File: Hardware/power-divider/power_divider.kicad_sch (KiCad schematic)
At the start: 22 parts

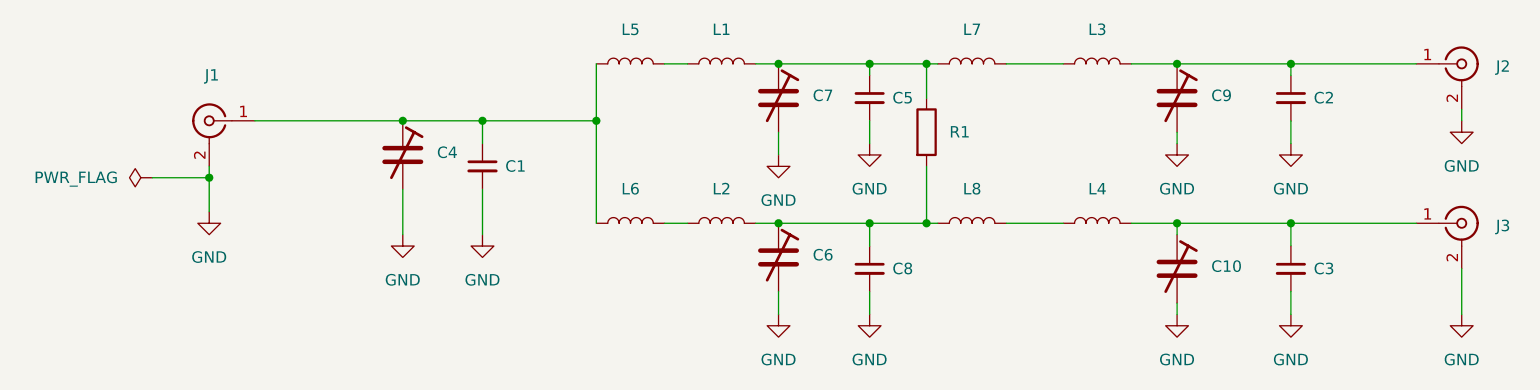
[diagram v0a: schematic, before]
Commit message: PD: Silkscreen Color Tweak
- Changed bottom silkscreen to green
- Aligned board edges and fill polygon to grid
- Rounded the corners
- Added box for label
- Moved R1 slightly closer
- Increased default netclass clearance from 0.2 to 0.6mm
- Set polygon clearance to 0 to fill to edge of holes
- Added SMA connector models
- Fixed Schematic-PCB parity
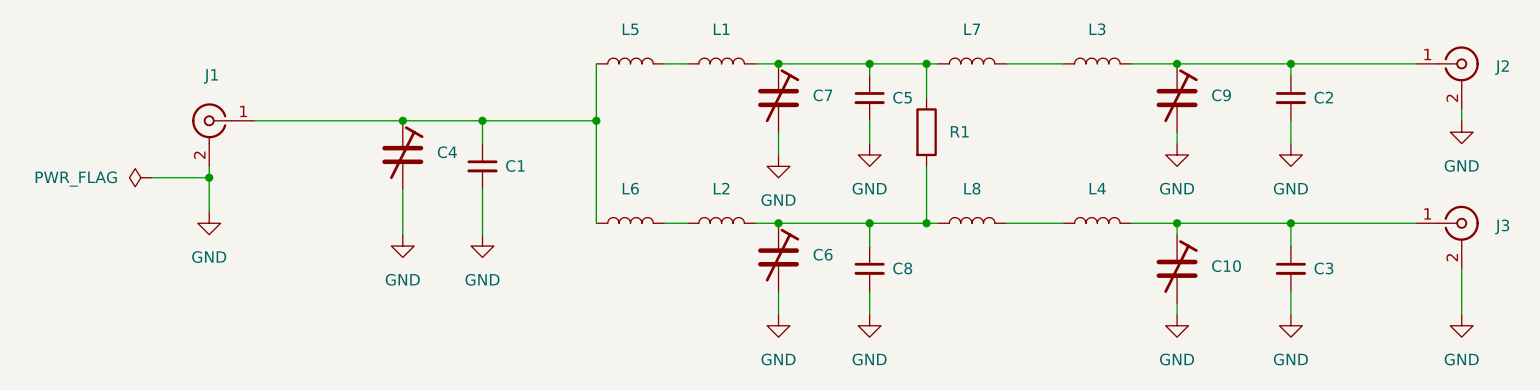
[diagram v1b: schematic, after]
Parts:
- C1, C2, C3: value (none) -> C_Small; footprint (none) -> Capacitor_SMD:C_0603_1608Metric
- C10, C4, C7, C9: value (none) -> C_Trim
- C5, C8: value (none) -> C_Small
- C6: value (none) -> v
- J1, J2, J3: value (none) -> Conn_Coaxial; footprint Connector_Coaxial:SMA_Samtec_SMA-J-P-X-ST-EM1_EdgeMount -> OTS_Tag:SMA_Samtec_SMA-J-P-X-ST-EM1_EdgeMount
- L1, L2, L3, L4, L5, L6, L7, L8: value (none) -> L
- R1: value (none) -> R
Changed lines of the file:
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@@
     (in_bom yes) (on_board yes) (fields_autoplaced)
     (property "Reference" "L3" (id 0) (at 133.35 111.76 90))
-    (property "Value" "" (id 1) (at 133.35 111.76 90)
+    (property "Value" "L" (id 1) (at 133.35 111.76 90)
       (effects (font (size 1.27 1.27)) hide)
     )
@@
       (effects (font (size 1.27 1.27)) (justify left))
     )
-    (property "Value" "" (id 1) (at 157.48 139.7062 0)
-      (effects (font (size 1.27 1.27)) (justify left) hide)
-    )
-    (property "Footprint" "" (id 2) (at 154.94 138.43 0)
+    (property "Value" "C_Small" (id 1) (at 157.48 139.7062 0)
+      (effects (font (size 1.27 1.27)) (justify left) hide)
+    )
+    (property "Footprint" "Capacitor_SMD:C_0603_1608Metric" (id 2) (at 154.94 138.43 0)
       (effects (font (size 1.27 1.27)) hide)
     )
@@
       (effects (font (size 1.27 1.27)) (justify left))
     )
-    (property "Value" "" (id 1) (at 157.48 120.6562 0)
-      (effects (font (size 1.27 1.27)) (justify left) hide)
-    )
-    (property "Footprint" "" (id 2) (at 154.94 119.38 0)
+    (property "Value" "C_Small" (id 1) (at 157.48 120.6562 0)
+      (effects (font (size 1.27 1.27)) (justify left) hide)
+    )
+    (property "Footprint" "Capacitor_SMD:C_0603_1608Metric" (id 2) (at 154.94 119.38 0)
       (effects (font (size 1.27 1.27)) hide)
     )
@@
       (effects (font (size 1.27 1.27)) (justify left))
     )
-    (property "Value" "" (id 1) (at 116.84 124.4599 0)
+    (property "Value" "R" (id 1) (at 116.84 124.4599 0)
       (effects (font (size 1.27 1.27)) (justify left) hide)
     )
@@
       (effects (font (size 1.27 1.27)) (justify left))
     )
-    (property "Value" "" (id 1) (at 174.9424 129.54 90)
-      (effects (font (size 1.27 1.27)) (justify left) hide)
-    )
-    (property "Footprint" "Connector_Coaxial:SMA_Samtec_SMA-J-P-X-ST-EM1_EdgeMount" (id 2) (at 173.99 133.35 0)
+    (property "Value" "Conn_Coaxial" (id 1) (at 174.9424 129.54 90)
+      (effects (font (size 1.27 1.27)) (justify left) hide)
+    )
+    (property "Footprint" "OTS_Tag:SMA_Samtec_SMA-J-P-X-ST-EM1_EdgeMount" (id 2) (at 173.99 133.35 0)
       (effects (font (size 1.27 1.27)) hide)
     )
@@
     (in_bom yes) (on_board yes) (fields_autoplaced)
     (property "Reference" "L1" (id 0) (at 91.44 111.76 90))
-    (property "Value" "" (id 1) (at 91.44 111.76 90)
+    (property "Value" "L" (id 1) (at 91.44 111.76 90)
       (effects (font (size 1.27 1.27)) hide)
     )
@@
     (in_bom yes) (on_board yes) (fields_autoplaced)
     (property "Reference" "L7" (id 0) (at 119.38 111.76 90))
-    (property "Value" "" (id 1) (at 119.38 111.76 90)
+    (property "Value" "L" (id 1) (at 119.38 111.76 90)
       (effects (font (size 1.27 1.27)) hide)
     )
@@
       (effects (font (size 1.27 1.27)) (justify left))
     )
-    (property "Value" "" (id 1) (at 176.53 117.1331 0)
-      (effects (font (size 1.27 1.27)) (justify left) hide)
-    )
-    (property "Footprint" "Connector_Coaxial:SMA_Samtec_SMA-J-P-X-ST-EM1_EdgeMount" (id 2) (at 173.99 115.57 0)
+    (property "Value" "Conn_Coaxial" (id 1) (at 176.53 117.1331 0)
+      (effects (font (size 1.27 1.27)) (justify left) hide)
+    )
+    (property "Footprint" "OTS_Tag:SMA_Samtec_SMA-J-P-X-ST-EM1_EdgeMount" (id 2) (at 173.99 115.57 0)
       (effects (font (size 1.27 1.27)) hide)
     )
@@
       (effects (font (size 1.27 1.27)) (justify left))
     )
-    (property "Value" "" (id 1) (at 101.6 138.1759 0)
+    (property "Value" "v" (id 1) (at 101.6 138.1759 0)
       (effects (font (size 1.27 1.27)) (justify left) hide)
     )
@@
     (in_bom yes) (on_board yes) (fields_autoplaced)
     (property "Reference" "L8" (id 0) (at 119.38 129.54 90))
-    (property "Value" "" (id 1) (at 119.38 129.54 90)
+    (property "Value" "L" (id 1) (at 119.38 129.54 90)
       (effects (font (size 1.27 1.27)) hide)
     )
@@
     (in_bom yes) (on_board yes) (fields_autoplaced)
     (property "Reference" "L2" (id 0) (at 91.44 129.54 90))
-    (property "Value" "" (id 1) (at 91.44 129.54 90)
+    (property "Value" "L" (id 1) (at 91.44 129.54 90)
       (effects (font (size 1.27 1.27)) hide)
     )
@@
     (in_bom yes) (on_board yes) (fields_autoplaced)
     (property "Reference" "J1" (id 0) (at 34.6074 116.84 0))
-    (property "Value" "" (id 1) (at 34.6074 116.84 0)
-      (effects (font (size 1.27 1.27)) hide)
-    )
-    (property "Footprint" "Connector_Coaxial:SMA_Samtec_SMA-J-P-X-ST-EM1_EdgeMount" (id 2) (at 34.29 121.92 0)
+    (property "Value" "Conn_Coaxial" (id 1) (at 34.6074 116.84 0)
+      (effects (font (size 1.27 1.27)) hide)
+    )
+    (property "Footprint" "OTS_Tag:SMA_Samtec_SMA-J-P-X-ST-EM1_EdgeMount" (id 2) (at 34.29 121.92 0)
       (effects (font (size 1.27 1.27)) hide)
     )
@@
       (effects (font (size 1.27 1.27)) (justify left))
     )
-    (property "Value" "" (id 1) (at 146.05 139.4459 0)
+    (property "Value" "C_Trim" (id 1) (at 146.05 139.4459 0)
       (effects (font (size 1.27 1.27)) (justify left) hide)
     )
@@
       (effects (font (size 1.27 1.27)) (justify left))
     )
-    (property "Value" "" (id 1) (at 59.69 126.7459 0)
+    (property "Value" "C_Trim" (id 1) (at 59.69 126.7459 0)
       (effects (font (size 1.27 1.27)) (justify left) hide)
     )
@@
     (in_bom yes) (on_board yes) (fields_autoplaced)
     (property "Reference" "L4" (id 0) (at 133.35 129.54 90))
-    (property "Value" "" (id 1) (at 133.35 129.54 90)
+    (property "Value" "L" (id 1) (at 133.35 129.54 90)
       (effects (font (size 1.27 1.27)) hide)
     )
@@
       (effects (font (size 1.27 1.27)) (justify left))
     )
-    (property "Value" "" (id 1) (at 110.49 139.7062 0)
+    (property "Value" "C_Small" (id 1) (at 110.49 139.7062 0)
       (effects (font (size 1.27 1.27)) (justify left) hide)
     )
@@
       (effects (font (size 1.27 1.27)) (justify left))
     )
-    (property "Value" "" (id 1) (at 67.31 128.2762 0)
-      (effects (font (size 1.27 1.27)) (justify left) hide)
-    )
-    (property "Footprint" "" (id 2) (at 64.77 127 0)
+    (property "Value" "C_Small" (id 1) (at 67.31 128.2762 0)
+      (effects (font (size 1.27 1.27)) (justify left) hide)
+    )
+    (property "Footprint" "Capacitor_SMD:C_0603_1608Metric" (id 2) (at 64.77 127 0)
       (effects (font (size 1.27 1.27)) hide)
     )
@@
     (in_bom yes) (on_board yes) (fields_autoplaced)
     (property "Reference" "L6" (id 0) (at 81.28 129.54 90))
-    (property "Value" "" (id 1) (at 81.28 129.54 90)
+    (property "Value" "L" (id 1) (at 81.28 129.54 90)
       (effects (font (size 1.27 1.27)) hide)
     )
@@
       (effects (font (size 1.27 1.27)) (justify left))
     )
-    (property "Value" "" (id 1) (at 110.49 120.6562 0)
+    (property "Value" "C_Small" (id 1) (at 110.49 120.6562 0)
       (effects (font (size 1.27 1.27)) (justify left) hide)
     )
@@
       (effects (font (size 1.27 1.27)) (justify left))
     )
-    (property "Value" "" (id 1) (at 101.6 120.3959 0)
+    (property "Value" "C_Trim" (id 1) (at 101.6 120.3959 0)
       (effects (font (size 1.27 1.27)) (justify left) hide)
     )
@@
     (in_bom yes) (on_board yes) (fields_autoplaced)
     (property "Reference" "L5" (id 0) (at 81.28 111.76 90))
-    (property "Value" "" (id 1) (at 81.28 111.76 90)
+    (property "Value" "L" (id 1) (at 81.28 111.76 90)
       (effects (font (size 1.27 1.27)) hide)
     )
@@
       (effects (font (size 1.27 1.27)) (justify left))
     )
-    (property "Value" "" (id 1) (at 146.05 120.3959 0)
+    (property "Value" "C_Trim" (id 1) (at 146.05 120.3959 0)
       (effects (font (size 1.27 1.27)) (justify left) hide)
     )
@@
     )
     (path "/8b31a9ad-c09d-47b9-beaa-1384fac3ffb7"
-      (reference "J1") (unit 1) (value "Conn_Coaxial") (footprint "Connector_Coaxial:SMA_Samtec_SMA-J-P-X-ST-EM1_EdgeMount")
+      (reference "J1") (unit 1) (value "Conn_Coaxial") (footprint "OTS_Tag:SMA_Samtec_SMA-J-P-X-ST-EM1_EdgeMount")
     )
     (path "/418e19cf-ec07-4213-bdc9-0796888f3d79"
-      (reference "J2") (unit 1) (value "Conn_Coaxial") (footprint "Connector_Coaxial:SMA_Samtec_SMA-J-P-X-ST-EM1_EdgeMount")
+      (reference "J2") (unit 1) (value "Conn_Coaxial") (footprint "OTS_Tag:SMA_Samtec_SMA-J-P-X-ST-EM1_EdgeMount")
     )
     (path "/30e8237d-252c-4464-afc5-907a1bec6c73"
-      (reference "J3") (unit 1) (value "Conn_Coaxial") (footprint "Connector_Coaxial:SMA_Samtec_SMA-J-P-X-ST-EM1_EdgeMount")
+      (reference "J3") (unit 1) (value "Conn_Coaxial") (footprint "OTS_Tag:SMA_Samtec_SMA-J-P-X-ST-EM1_EdgeMount")
     )
     (path "/32a267be-7d09-4fc0-92b3-879ef08c2c00"
